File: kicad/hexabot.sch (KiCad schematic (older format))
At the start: 102 parts, among them P1 BATTERY, P10 BUMP2, P11 USB_B, P12 DEBUG, P13 NC, P14 MOTOR_R, P15 MOTOR_L, P16 UART1_5V, P17 ENC1, P18 ENC2, P19 ENC3, P2 EXT_POWER, P20 ENC4, P21 UART2_FTDI3V3, P22 NC, P23 START, P24 DYNAMIXEL2, P25 NC, P26 NC, P27 NC, P3 SERVO1, P4 SERVO2, P5 DYNAMIXEL1, P6 PICKIT, P7 PANIC BUTTON, P8 NC, P9 BUMP1, Q1 Q_NMOS_GSD, Q2 Q_NMOS_GSD, Q3 Q_NMOS_GSD, Q4 Q_NMOS_GSD, SW1 PUSH1, SW2 PUSH2, U1 PTN78020 +5V, U2 PTN78020 SERVO, U3 MCP1727, U4 DSPIC33EP256MU806, Y1 8M

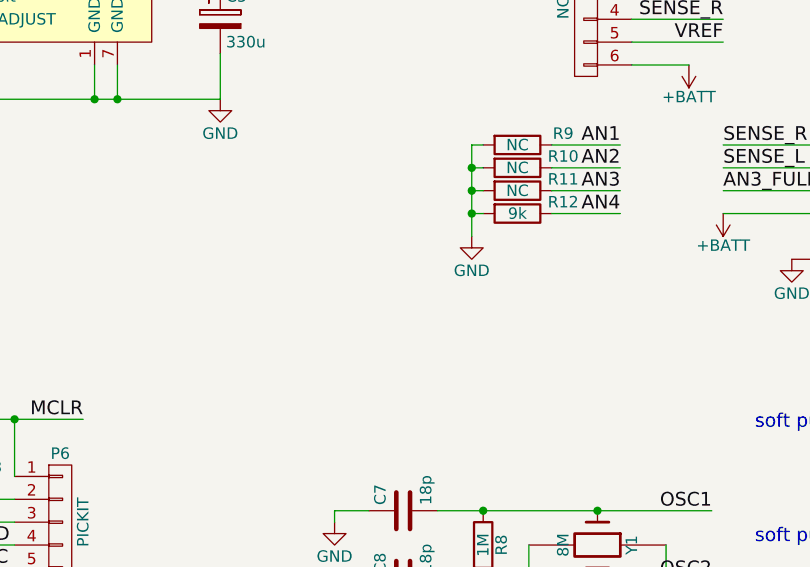
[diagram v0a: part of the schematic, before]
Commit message: Add TODOs to improve VSENSE
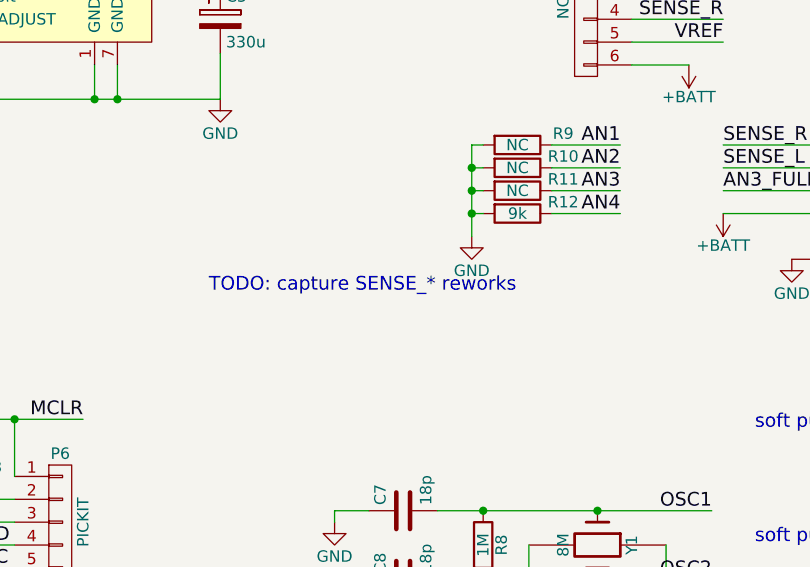
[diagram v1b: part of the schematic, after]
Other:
- note added: "TODO: capture SENSE_* reworks"
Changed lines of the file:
@@
 	3150 7500 3150 7000
 Connection ~ 3150 7000
+Text Notes 2500 4900 0    60   ~ 0
+TODO: capture SENSE_* reworks
 $EndSCHEMATC
